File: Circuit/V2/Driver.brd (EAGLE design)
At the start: 84.5 x 61.9 mm, 36 parts

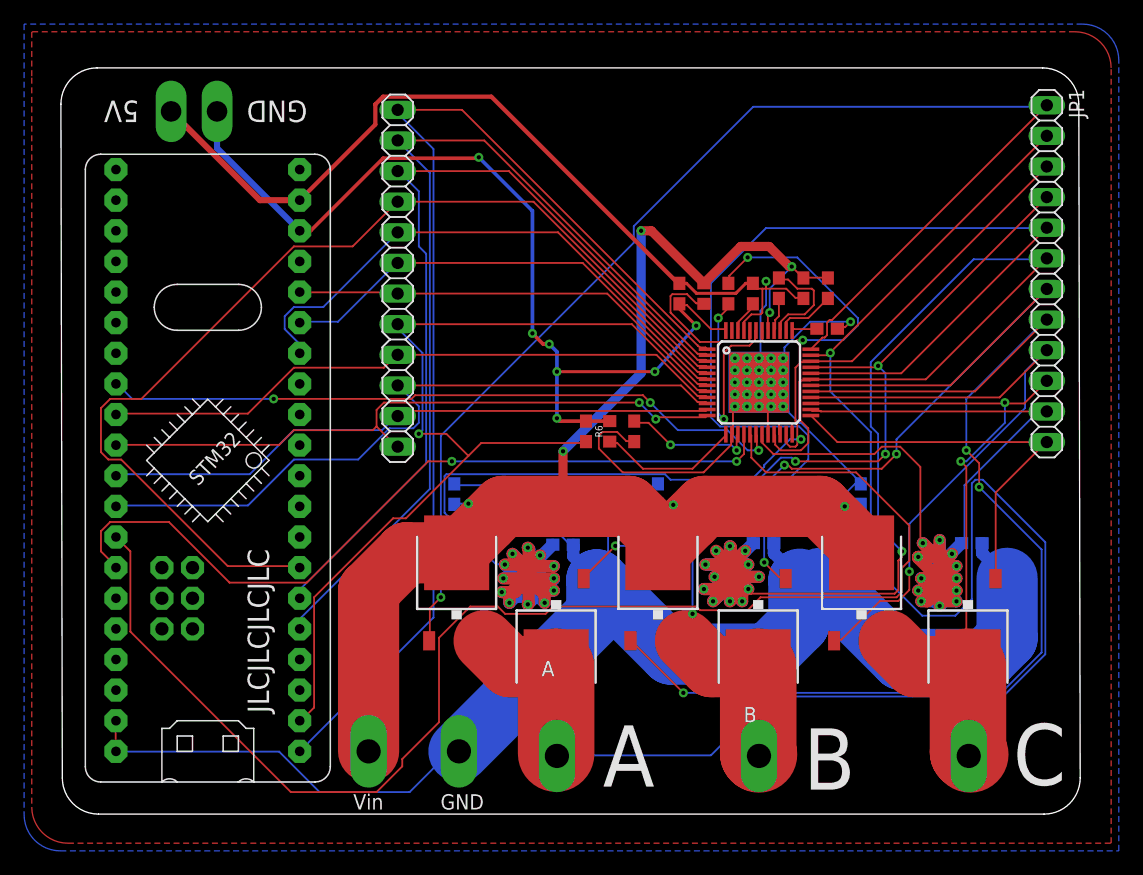
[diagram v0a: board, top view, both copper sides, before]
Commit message: Designed and auto routed BLDC driver V2 circuit
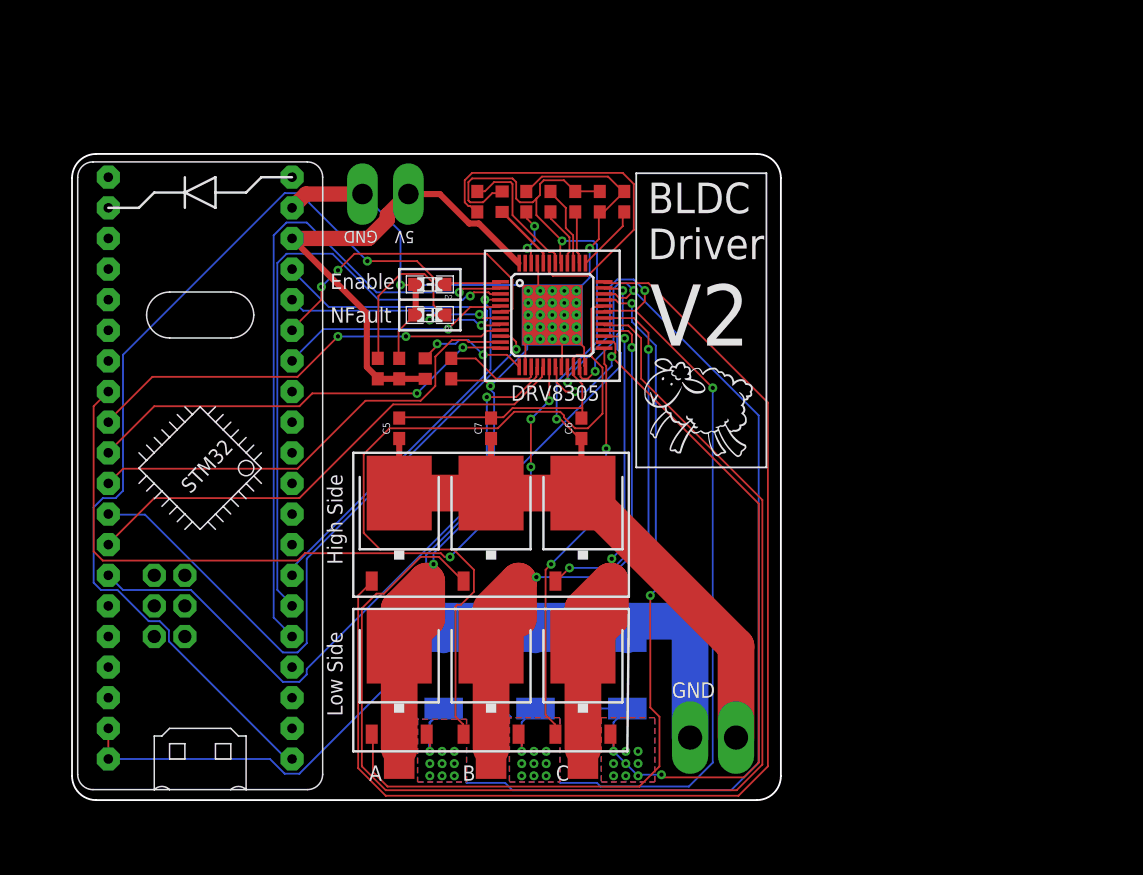
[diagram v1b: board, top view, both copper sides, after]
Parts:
- removed JP1, JP2: (no value), pinhead:1X12
- removed U$2, U$4, U$5, U$6, U$7, U$8: IRLR7843, BLDC project:TO252
- added D1, D2: (no value), standardparts:0805.LED
- added HA, HB, HC, LA, LB, LC: IRLR7843, BLDC project:TO252
- A, B, C: value PTR1PAD1-20Y -> (none); device testpad:P1-20Y -> wirepad:SMD2,54-5,08
- moved C4 34.1 mm to (43.2, 10.8), turned to 270 degrees
- moved C 32.0 mm to (43.2, 4.70)
- moved C7 31.2 mm to (35.6, 31.2), flipped to the top
- moved TP1 30.5 mm to (55.9, 5.59)
- moved R5 29.8 mm to (46.9, 10.8), turned to 270 degrees
- moved C3 25.2 mm to (35.6, 10.7), turned to 270 degrees
- moved C16 24.1 mm to (27.9, 36.2)
- moved B 22.2 mm to (35.6, 4.70)
- moved C14 22.2 mm to (34.4, 50.0)
- moved C11 22.1 mm to (42.5, 50.0)
- moved R2 20.7 mm to (39.2, 10.8), turned to 270 degrees
- moved C15 20.3 mm to (38.5, 50.0)
- moved C13 20.3 mm to (40.5, 50.0)
- moved C10 19.9 mm to (46.6, 50.0), turned to 90 degrees
- moved TP2 19.2 mm to (52.1, 5.59)
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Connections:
- net GH_A: now also HA.1; no longer JP1.1, U$2.1
- net GH_B: now also HB.1; no longer JP1.8, U$5.1
- net GH_C: now also HC.1; no longer JP1.9, U$7.1
- net GL_A: now also LA.1; no longer JP1.4, U$4.1
- net GL_B: now also LB.1; no longer JP1.5, U$6.1
- net GL_C: now also LC.1; no longer JP1.12, U$8.1
- net GND: now also D1.P$2, D2.P$2
- net PA10: no longer JP2.9
- net PA4: no longer JP2.4
- net PA5: no longer JP2.1
- net PA6: no longer JP2.2
- net PA7: no longer JP2.3
- net PA8: no longer JP2.11
- net PA9: no longer JP2.10
- net PB12: now also D2.P$1; no longer JP2.12
- net PB13: no longer JP2.5, R6.2, U$3.8
- net PB6: no longer JP2.8
- net PB7: no longer JP2.7
- net PB8: no longer JP2.6
- net PB9: now also D1.P$1, R6.2, U$3.8
- net SH_A: now also A.1, HA.2, LA.3; no longer A.TP, JP1.2, U$2.2, U$4.3
- net SH_B: now also B.1, HB.2, LB.3; no longer B.TP, JP1.7, U$5.2, U$6.3
- net SH_C: now also C.1, HC.2, LC.3; no longer C.TP, JP1.10, U$7.2, U$8.3
- net SN1: now also LA.2; no longer JP1.3, U$4.2
- net SN2: now also LB.2; no longer JP1.6, U$6.2
- net SN3: now also LC.2; no longer JP1.11, U$8.2
- net VIN: now also HA.3, HB.3, HC.3; no longer U$2.3, U$5.3, U$7.3
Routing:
- net SH_A: track 142.5 -> 58.2 mm, vias 1 -> 2
- net PB13: track 81.7 -> 0.00 mm, vias 1 -> 0
- net PB0: track 113.1 -> 42.7 mm
- net GND: track 318.3 -> 251.9 mm, vias 2 -> 3
- net SN2: track 138.5 -> 81.5 mm, vias 13 -> 12
- net PA10: track 87.2 -> 31.2 mm, vias 0 -> 1
- net SN1: track 142.2 -> 93.9 mm, vias 13 -> 11
- net PB9: track 0.00 -> 40.6 mm, vias 0 -> 2
- net SN3: track 113.1 -> 72.9 mm
- net VCC: track 79.8 -> 41.6 mm, vias 7 -> 0
- net SH_B: track 84.0 -> 55.8 mm, vias 3 -> 2
- net PB6: track 46.4 -> 19.2 mm, vias 0 -> 1
- net GH_C: track 53.8 -> 27.7 mm, vias 1 -> 2
- net VIN: track 125.8 -> 101.5 mm, vias 7 -> 2
- net GL_B: track 88.6 -> 64.3 mm, vias 1 -> 0
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- added copper zone on layer 1, net SN1
- added copper zone on layer 16, net SN1
- added copper zone on layer 1, net SN2
- added copper zone on layer 16, net SN2
- added copper zone on layer 1, net SN3
- added copper zone on layer 16, net SN3
- removed copper zone on layer 16, net B
- removed copper zone on layer 1, net D
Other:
- board size 84.5 x 61.9 mm -> 58.8 x 53.6 mm
- board text added: "BLDC Driver"
- board text added: "DRV8305"
- board text added: "Enable"
- board text added: "High Side"
- board text added: "Low Side"
- board text added: "NFault"
- board text added: "V2"
- board text removed: "A"
- board text removed: "B"
- board text removed: "C"
- board text removed: "JLCJLCJLCJLC"
- board text removed: "Vin"

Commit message: Deleted all the autorouting signal
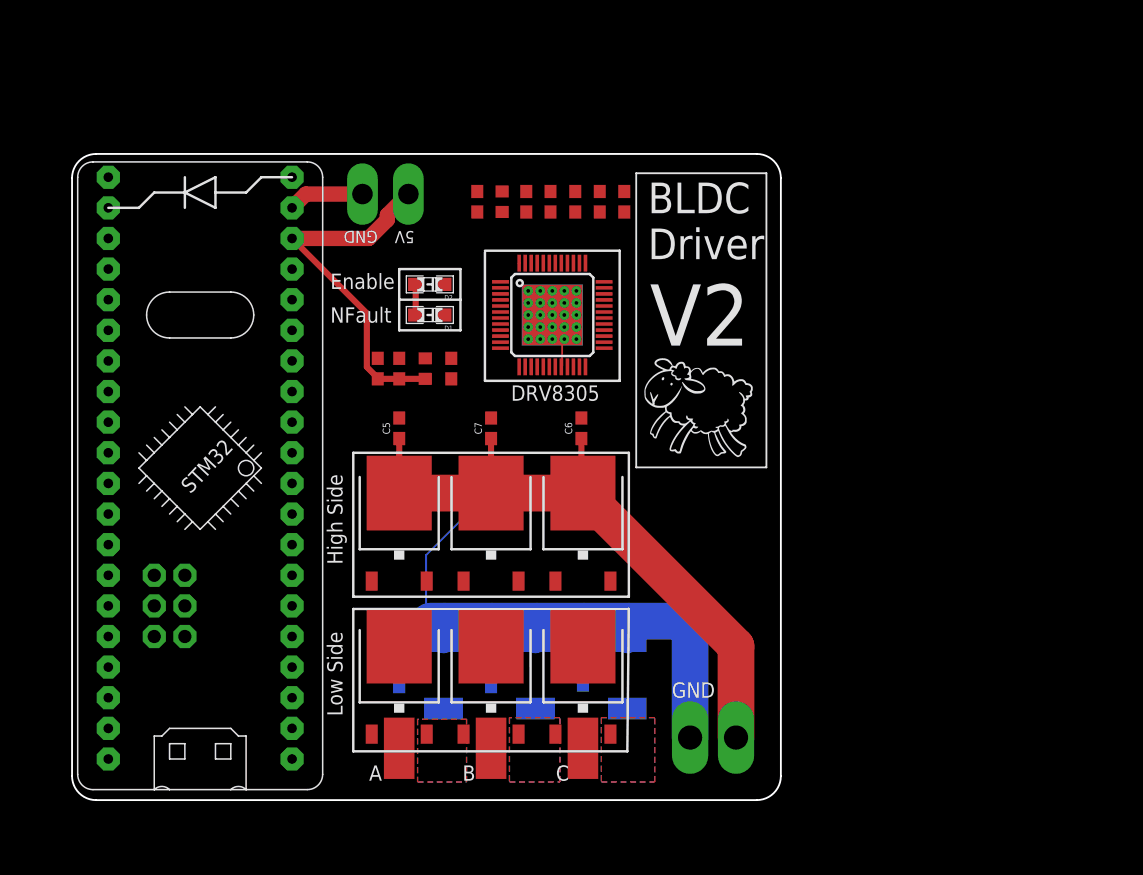
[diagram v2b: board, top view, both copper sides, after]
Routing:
- net GND: track 251.9 -> 100.8 mm, vias 3 -> 0
- net GH_B: track 102.2 -> 0.00 mm
- net GH_A: track 99.9 -> 0.00 mm
- net SN1: track 93.9 -> 0.00 mm, vias 11 -> 0
- net PB12: track 83.7 -> 0.00 mm, vias 1 -> 0
- net SN2: track 81.5 -> 0.00 mm, vias 12 -> 0
- net SN3: track 72.9 -> 0.00 mm, vias 12 -> 0
- net GL_A: track 70.3 -> 0.00 mm, vias 2 -> 0
- net GL_B: track 64.3 -> 0.00 mm
- net PA3: track 63.2 -> 0.00 mm, vias 4 -> 0
- net SH_A: track 58.2 -> 0.00 mm, vias 2 -> 0
- net SH_B: track 55.8 -> 0.00 mm, vias 2 -> 0
- net PA8: track 55.7 -> 0.00 mm, vias 1 -> 0
- net PA7: track 55.2 -> 0.00 mm, vias 1 -> 0
- net PB1: track 55.2 -> 0.00 mm, vias 1 -> 0
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
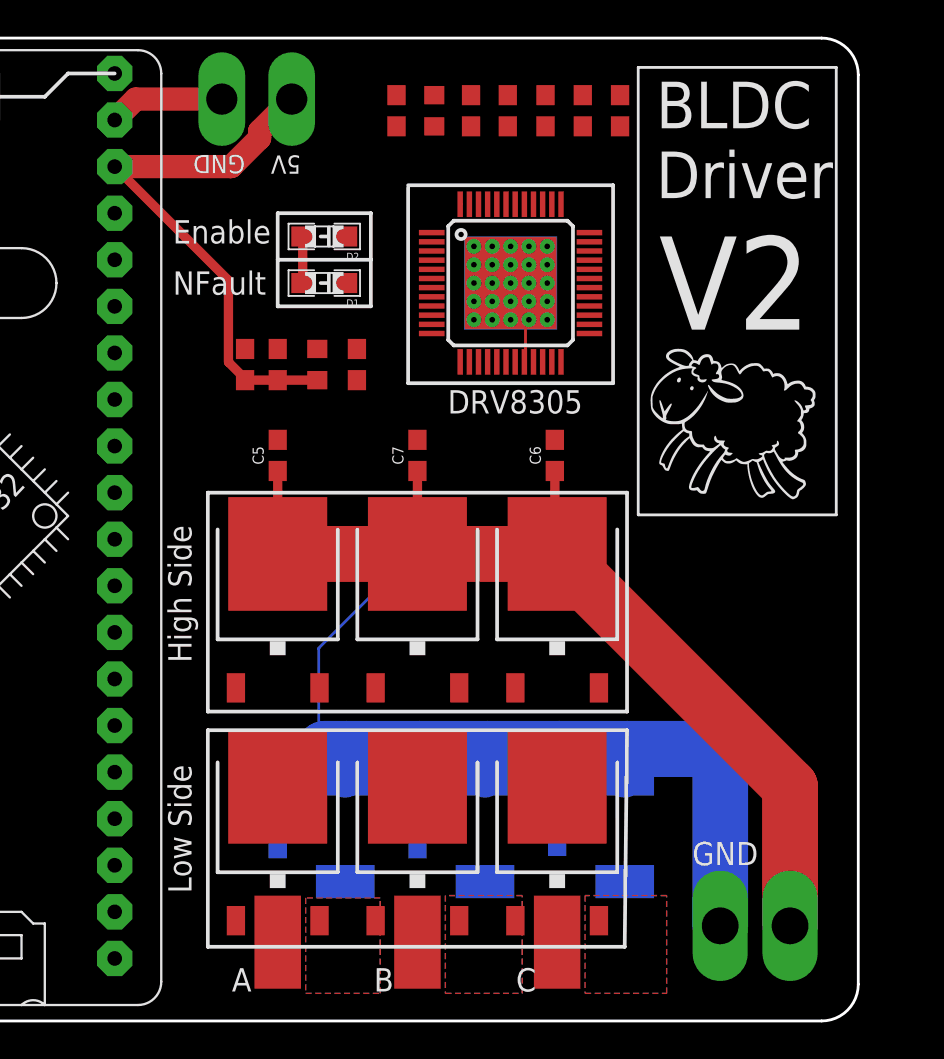
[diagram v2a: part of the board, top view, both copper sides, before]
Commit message: Manually routed the Shunt resistor detection signal to the Gate driver
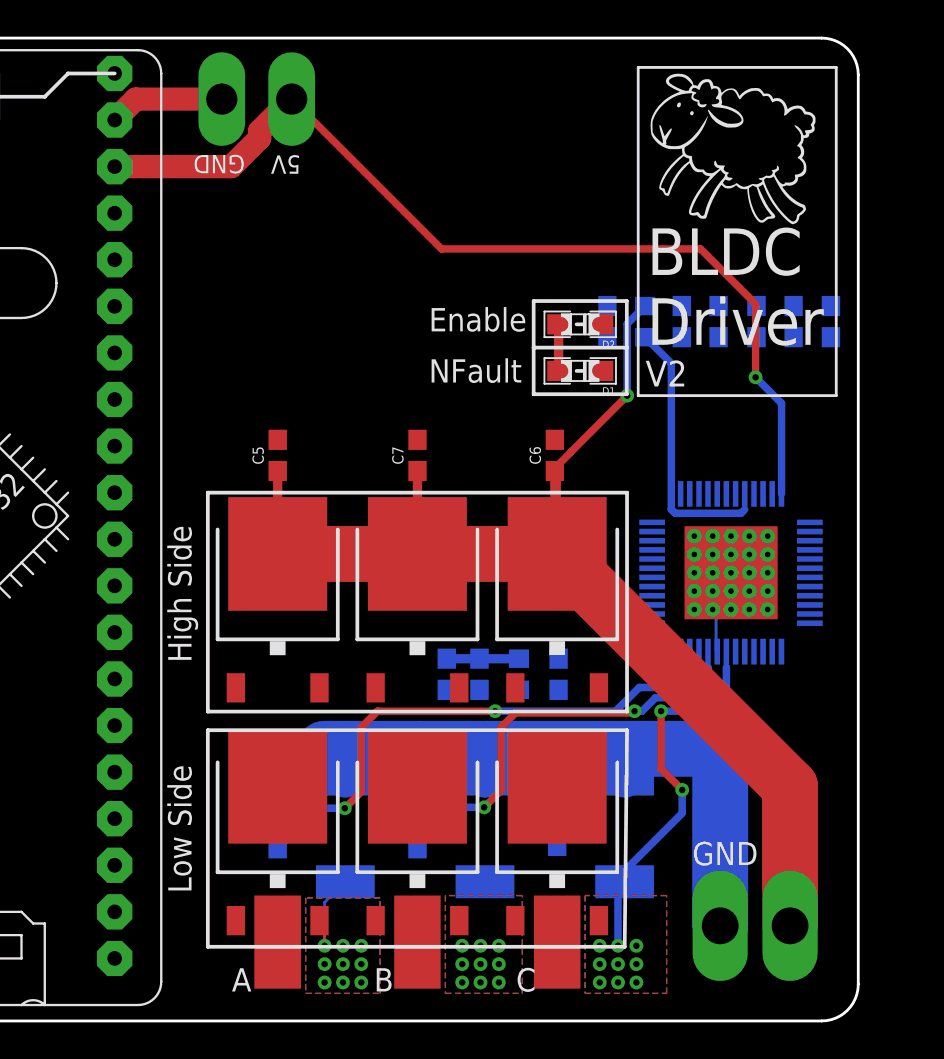
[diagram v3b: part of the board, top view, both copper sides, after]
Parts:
- moved C1 20.2 mm to (43.3, 19.3), flipped to the bottom, turned to 90 degrees
- moved R6 20.2 mm to (37.2, 19.3), flipped to the bottom, turned to 270 degrees
- moved C16 20.2 mm to (38.9, 19.3), flipped to the bottom, turned to 270 degrees
- moved R3 20.2 mm to (41.1, 19.3), flipped to the bottom, turned to 270 degrees
- moved U$3 19.9 mm to (52.7, 24.8), flipped to the bottom
- moved C10 16.3 mm to (58.1, 38.5), flipped to the bottom
- moved C11 16.3 mm to (54.0, 38.5), flipped to the bottom
- moved C12 16.3 mm to (56.1, 38.5), flipped to the bottom
- moved C13 16.3 mm to (52.0, 38.5), flipped to the bottom
- moved C14 16.3 mm to (45.9, 38.5), flipped to the bottom
- moved C15 16.3 mm to (50.0, 38.5), flipped to the bottom
- moved R4 16.3 mm to (48.0, 38.5), flipped to the bottom
- moved D1 14.8 mm to (44.4, 35.8)
- moved D2 14.8 mm to (44.4, 38.4)
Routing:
- net SN1: track 0.00 -> 35.1 mm, vias 0 -> 11
- net VCC: track 30.1 -> 56.4 mm, vias 0 -> 1
- net SN2: track 0.00 -> 22.0 mm, vias 0 -> 11
- net SN3: track 0.00 -> 19.9 mm, vias 0 -> 11
- net VIN: track 54.4 -> 69.9 mm, vias 0 -> 1
- net VDRAIN: track 0.00 -> 14.2 mm
- net GND: track 100.8 -> 88.8 mm

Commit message: Fix some routering bug
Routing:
- net VDRAIN: track 14.2 -> 10.8 mm
- net SN2: track 22.0 -> 22.9 mm
- net SN3: track 19.9 -> 20.8 mm
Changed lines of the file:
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@@
 <drawing>
 <settings>
-<setting alwaysvectorfont="yes"/>
+<setting alwaysvectorfont="no"/>
 <setting verticaltext="up"/>
 </settings>
@@
 <wire x1="53.66" y1="23.84" x2="54.66" y2="23.84" width="0.1524" layer="1"/>
 <wire x1="56.077" y1="37.688" x2="58.109" y2="39.388" width="0" layer="19" extent="16-16"/>
-<wire x1="49.981" y1="39.388" x2="56.077" y2="37.688" width="0" layer="19" extent="16-16"/>
+<wire x1="56.077" y1="37.688" x2="49.981" y2="39.388" width="0" layer="19" extent="16-16"/>
 <wire x1="43.262" y1="38.389" x2="49.981" y2="39.388" width="0" layer="19" extent="1-16"/>
 <wire x1="43.053" y1="32.092" x2="43.262" y2="35.849" width="0" layer="19" extent="1-1"/>
@@
 <wire x1="48.84775625" y1="17.2946" x2="51.0946" y2="17.2946" width="0.4064" layer="16"/>
 <wire x1="51.0946" y1="17.2946" x2="52.41" y2="18.61" width="0.4064" layer="16"/>
-<wire x1="52.41" y1="19.68710625" x2="52.41" y2="20.54" width="0" layer="19" extent="16-16"/>
+<wire x1="52.41" y1="19.68710625" x2="52.41" y2="20.54" width="0.3" layer="16"/>
+<wire x1="52.41" y1="20.54" x2="48.36" y2="22.59" width="0" layer="19" extent="16-16"/>
+<wire x1="47.5" y1="4.5" x2="46.5" y2="4.5" width="0" layer="19" extent="1-1"/>
+<wire x1="46.5" y1="3.5" x2="46.5" y2="4.5" width="0" layer="19" extent="1-1"/>
+<wire x1="47.5" y1="3.5" x2="47.5" y2="4.5" width="0" layer="19" extent="1-1"/>
+<wire x1="45.5" y1="4.5" x2="46.5" y2="4.5" width="0" layer="19" extent="1-1"/>
+<wire x1="45.5" y1="3.5" x2="46.5" y2="3.5" width="0" layer="19" extent="1-1"/>
+<wire x1="46.5" y1="2.5" x2="46.5" y2="3.5" width="0" layer="19" extent="1-1"/>
+<wire x1="47.5" y1="2.5" x2="47.5" y2="3.5" width="0" layer="19" extent="1-1"/>
+<wire x1="45.5" y1="2.5" x2="45.5" y2="3.5" width="0" layer="19" extent="1-1"/>
+<wire x1="45.46" y1="5.868" x2="45.5" y2="4.5" width="0" layer="19" extent="1-1"/>
+<wire x1="46.863" y1="7.995" x2="45.46" y2="5.868" width="0" layer="19" extent="1-16"/>
 <wire x1="43.18" y1="9.945" x2="46.863" y2="7.995" width="0" layer="19" extent="16-16"/>
-<wire x1="48.36" y1="22.59" x2="52.41" y2="20.54" width="0" layer="19" extent="16-16"/>
 </signal>
 <signal name="SH_C">
@@
 <wire x1="47.81000625" y1="17.2946" x2="47.4" y2="17.2946" width="0.4064" layer="16"/>
 <wire x1="48.54380625" y1="18.0284" x2="47.81000625" y2="17.2946" width="0.4064" layer="16"/>
-<wire x1="51.41" y1="19.61" x2="49.8284" y2="18.0284" width="0.4064" layer="16"/>
+<wire x1="49.8284" y1="18.0284" x2="51.41" y2="19.61" width="0.4064" layer="16"/>
 <wire x1="49.8284" y1="18.0284" x2="48.54380625" y2="18.0284" width="0.4064" layer="16"/>
 <wire x1="47.4" y1="17.2946" x2="47.3054" y2="17.2" width="0.4064" layer="1"/>
 <wire x1="47.3054" y1="17.2" x2="40.90910625" y2="17.2" width="0.4064" layer="1"/>
-<wire x1="51.41" y1="19.68710625" x2="51.41" y2="20.54" width="0" layer="19" extent="16-16"/>
+<wire x1="51.41" y1="19.61" x2="51.41" y2="20.54" width="0.3" layer="16"/>
+<wire x1="51.41" y1="20.54" x2="48.36" y2="25.09" width="0" layer="19" extent="16-16"/>
 <wire x1="39.243" y1="7.995" x2="39.2" y2="12.0484" width="0" layer="19" extent="16-16"/>
-<wire x1="48.36" y1="25.09" x2="51.41" y2="20.54" width="0" layer="19" extent="16-16"/>
+<wire x1="37.84" y1="5.868" x2="39.243" y2="7.995" width="0" layer="19" extent="1-16"/>
+<wire x1="38" y1="4.5" x2="37.84" y2="5.868" width="0" layer="19" extent="1-1"/>
+<wire x1="39" y1="4.5" x2="38" y2="4.5" width="0" layer="19" extent="1-1"/>
+<wire x1="40" y1="4.5" x2="39" y2="4.5" width="0" layer="19" extent="1-1"/>
+<wire x1="39" y1="3.5" x2="39" y2="4.5" width="0" layer="19" extent="1-1"/>
+<wire x1="40" y1="3.5" x2="40" y2="4.5" width="0" layer="19" extent="1-1"/>
+<wire x1="38" y1="3.5" x2="38" y2="4.5" width="0" layer="19" extent="1-1"/>
+<wire x1="39" y1="2.5" x2="39" y2="3.5" width="0" layer="19" extent="1-1"/>
+<wire x1="40" y1="2.5" x2="40" y2="3.5" width="0" layer="19" extent="1-1"/>
+<wire x1="38" y1="2.5" x2="38" y2="3.5" width="0" layer="19" extent="1-1"/>
 </signal>
 <signal name="GL_B">
@@
 <contactref element="U$3" pad="44"/>
 <contactref element="R4" pad="1"/>
-<wire x1="49.4044" y1="28.29270625" x2="49.61270625" y2="28.0844" width="0.4064" layer="16"/>
-<wire x1="53.20729375" y1="28.0844" x2="53.41" y2="28.28710625" width="0.4064" layer="16"/>
-<wire x1="49.61270625" y1="28.0844" x2="53.20729375" y2="28.0844" width="0.4064" layer="16"/>
-<wire x1="47.977" y1="37.688" x2="49.4044" y2="36.2606" width="0.4064" layer="16"/>
-<wire x1="49.4044" y1="36.2606" x2="49.4044" y2="28.29270625" width="0.4064" layer="16"/>
-<wire x1="53.41" y1="28.28710625" x2="53.41" y2="29.14" width="0" layer="19" extent="16-16"/>
+<wire x1="47.977" y1="37.688" x2="53.41" y2="32.255" width="0.254" layer="16"/>
+<wire x1="53.41" y1="32.255" x2="53.41" y2="29.14" width="0.254" layer="16"/>
 </signal>
 <signal name="DVDD">
@@
 <wire x1="32.5044" y1="16.41529375" x2="33.38370625" y2="17.2946" width="0.4064" layer="1"/>
 <wire x1="33.38370625" y1="17.2946" x2="39.8" y2="17.2946" width="0.4064" layer="1"/>
-<wire x1="50.41" y1="20.54" x2="50.4" y2="20.53" width="0.4064" layer="16"/>
-<wire x1="50.4" y1="20.53" x2="50.4" y2="19.4" width="0.4064" layer="16"/>
+<wire x1="50.41" y1="20.54" x2="50.4" y2="20.53" width="0.3" layer="16"/>
+<wire x1="50.4" y1="20.53" x2="50.4" y2="19.4" width="0.3" layer="16"/>
 <wire x1="50.4" y1="19.4" x2="49.5872" y2="18.5872" width="0.4064" layer="16"/>
 <wire x1="49.5872" y1="18.5872" x2="47.65485" y2="18.5872" width="0.4064" layer="16"/>
@@
 <wire x1="50.41" y1="20.54" x2="48.36" y2="26.59" width="0" layer="19" extent="16-16"/>
 <wire x1="31.623" y1="7.995" x2="31.6" y2="12" width="0" layer="19" extent="16-16"/>
+<wire x1="31.5" y1="4.5" x2="30.5" y2="4.5" width="0" layer="19" extent="1-1"/>
+<wire x1="32.5" y1="4.5" x2="31.5" y2="4.5" width="0" layer="19" extent="1-1"/>
+<wire x1="30.5" y1="3.5" x2="30.5" y2="4.5" width="0" layer="19" extent="1-1"/>
+<wire x1="31.5" y1="3.5" x2="31.5" y2="4.5" width="0" layer="19" extent="1-1"/>
+<wire x1="32.5" y1="3.5" x2="32.5" y2="4.5" width="0" layer="19" extent="1-1"/>
+<wire x1="30.5" y1="2.5" x2="30.5" y2="3.5" width="0" layer="19" extent="1-1"/>
+<wire x1="31.5" y1="2.5" x2="31.5" y2="3.5" width="0" layer="19" extent="1-1"/>
+<wire x1="32.5" y1="2.5" x2="32.5" y2="3.5" width="0" layer="19" extent="1-1"/>
 </signal>
 <signal name="PWRGD">
